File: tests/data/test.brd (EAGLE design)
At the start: 15.9 x 10.2 mm, 2 parts

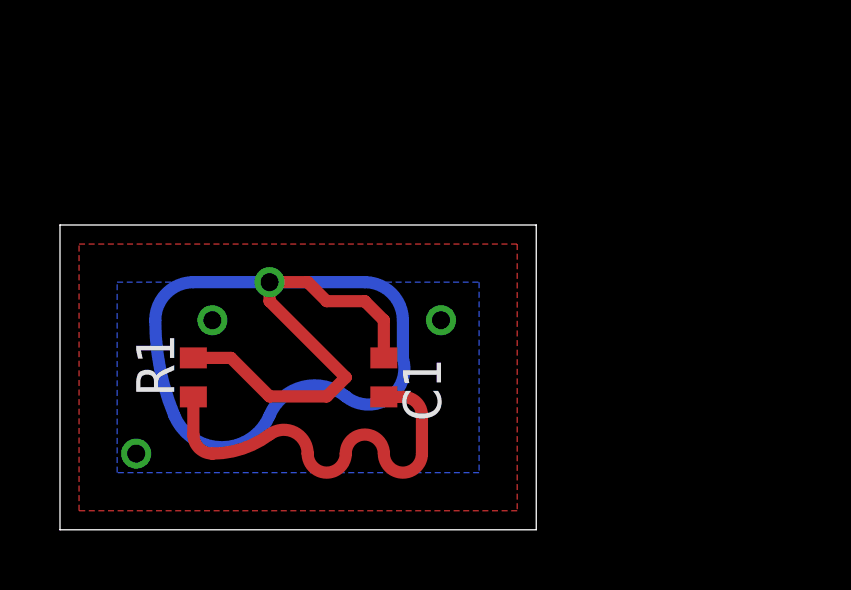
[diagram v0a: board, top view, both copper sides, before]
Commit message: Fix text center align (#14)
* Update test to detect text align error

* Treat align 'center' as 'center-center'
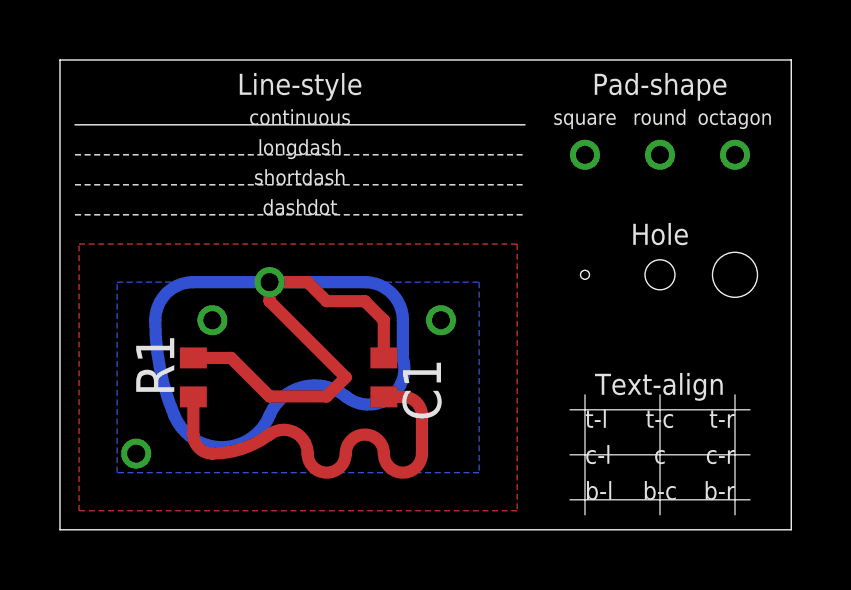
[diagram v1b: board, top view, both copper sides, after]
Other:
- board size 15.9 x 10.2 mm -> 24.4 x 15.7 mm
- board text added: "Hole"
- board text added: "Line-style"
- board text added: "Pad-shape"
- board text added: "Text-align"
- board text added: "b-c"
- board text added: "b-l"
- board text added: "b-r"
- board text added: "c"
- board text added: "c-l"
- board text added: "c-r"
- board text added: "continuous"
- board text added: "dashdot"
- board text added: "longdash"
- board text added: "octagon"
- board text added: "round"
- board text added: "shortdash"
- board text added: "square"
- board text added: "t-c"
- board text added: "t-l"
- board text added: "t-r"
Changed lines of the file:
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@@
 <setting verticaltext="up"/>
 </settings>
-<grid distance="0.05" unitdist="inch" unit="inch" style="lines" multiple="1" display="no" altdistance="0.025" altunitdist="inch" altunit="inch"/>
+<grid distance="0.5" unitdist="mm" unit="mm" style="lines" multiple="1" display="no" altdistance="0.025" altunitdist="inch" altunit="inch"/>
 <layers>
 <layer number="1" name="Top" color="4" fill="1" visible="yes" active="yes"/>
@@
 <layer number="43" name="vRestrict" color="2" fill="10" visible="yes" active="yes"/>
 <layer number="44" name="Drills" color="7" fill="1" visible="no" active="yes"/>
-<layer number="45" name="Holes" color="7" fill="1" visible="no" active="yes"/>
+<layer number="45" name="Holes" color="7" fill="1" visible="yes" active="yes"/>
 <layer number="46" name="Milling" color="3" fill="1" visible="no" active="yes"/>
 <layer number="47" name="Measures" color="7" fill="1" visible="no" active="yes"/>
@@
 <board>
 <plain>
-<wire x1="0" y1="0" x2="15.875" y2="0" width="0" layer="20"/>
-<wire x1="15.875" y1="0" x2="15.875" y2="10.16" width="0" layer="20"/>
-<wire x1="15.875" y1="10.16" x2="0" y2="10.16" width="0" layer="20"/>
-<wire x1="0" y1="10.16" x2="0" y2="0" width="0" layer="20"/>
+<wire x1="0" y1="0" x2="24.375" y2="0" width="0" layer="20"/>
+<wire x1="24.375" y1="0" x2="24.375" y2="15.66" width="0" layer="20"/>
+<wire x1="24.375" y1="15.66" x2="0" y2="15.66" width="0" layer="20"/>
+<wire x1="0" y1="15.66" x2="0" y2="0" width="0" layer="20"/>
+<text x="17.5" y="4" size="0.6" layer="21" align="top-left">t-l</text>
+<wire x1="17.5" y1="4.5" x2="17.5" y2="0.5" width="0.02" layer="21"/>
+<wire x1="20" y1="4.5" x2="20" y2="0.5" width="0.02" layer="21"/>
+<wire x1="22.5" y1="4.5" x2="22.5" y2="0.5" width="0.02" layer="21"/>
+<wire x1="17" y1="4" x2="23" y2="4" width="0.02" layer="21"/>
+<wire x1="17" y1="2.5" x2="23" y2="2.5" width="0.02" layer="21"/>
+<wire x1="17" y1="1" x2="23" y2="1" width="0.02" layer="21"/>
+<text x="17.5" y="2.5" size="0.6" layer="21" align="center-left">c-l</text>
+<text x="17.5" y="1" size="0.6" layer="21">b-l</text>
+<text x="20" y="4" size="0.6" layer="21" align="top-center">t-c</text>
+<text x="20" y="2.5" size="0.6" layer="21" align="center">c</text>
+<text x="20" y="1" size="0.6" layer="21" align="bottom-center">b-c</text>
+<text x="22.5" y="4" size="0.6" layer="21" align="top-right">t-r</text>
+<text x="22.5" y="2.5" size="0.6" layer="21" align="center-right">c-r</text>
+<text x="22.5" y="1" size="0.6" layer="21" align="bottom-right">b-r</text>
+<text x="20" y="4.5" size="0.7" layer="21" align="bottom-center">Text-align</text>
+<text x="8" y="14.5" size="0.7" layer="21" align="bottom-center">Line-style</text>
+<wire x1="0.5" y1="12.5" x2="15.5" y2="12.5" width="0.05" layer="21" style="longdash"/>
+<wire x1="0.5" y1="11.5" x2="15.5" y2="11.5" width="0.05" layer="21" style="shortdash"/>
+<wire x1="0.5" y1="10.5" x2="15.5" y2="10.5" width="0.05" layer="21" style="dashdot"/>
+<wire x1="0.5" y1="13.5" x2="15.5" y2="13.5" width="0.05" layer="21"/>
+<text x="8" y="13.5" size="0.5" layer="21" align="bottom-center">continuous</text>
+<text x="8" y="12.5" size="0.5" layer="21" align="bottom-center">longdash</text>
+<text x="8" y="11.5" size="0.5" layer="21" align="bottom-center">shortdash</text>
+<text x="8" y="10.5" size="0.5" layer="21" align="bottom-center">dashdot</text>
+<text x="20" y="14.5" size="0.7" layer="21" align="bottom-center">Pad-shape</text>
+<text x="17.5" y="13.5" size="0.5" layer="21" align="bottom-center">square</text>
+<text x="20" y="13.5" size="0.5" layer="21" align="bottom-center">round</text>
+<text x="22.5" y="13.5" size="0.5" layer="21" align="bottom-center">octagon</text>
+<hole x="20" y="8.5" drill="1"/>
+<text x="20" y="9.5" size="0.7" layer="21" align="bottom-center">Hole</text>
+<hole x="17.5" y="8.5" drill="0.3"/>
+<hole x="22.5" y="8.5" drill="1.5"/>
 </plain>
 <attributes>
@@
 <vertex x="1.905" y="1.905"/>
 </polygon>
-<via x="2.54" y="2.54" extent="1-16" drill="0.6" shape="octagon"/>
+<via x="2.54" y="2.54" extent="1-16" drill="0.6"/>
 <via x="12.7" y="6.985" extent="1-16" drill="0.6"/>
 <via x="5.08" y="6.985" extent="1-16" drill="0.6"/>
 </signal>
+<signal name="N$3">
+<via x="17.5" y="12.5" extent="1-16" drill="0.6" shape="square"/>
+</signal>
+<signal name="N$4">
+<via x="20" y="12.5" extent="1-16" drill="0.6"/>
+</signal>
+<signal name="N$5">
+<via x="22.5" y="12.5" extent="1-16" drill="0.6" shape="octagon"/>
+</signal>
 </signals>

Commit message: Support long pad (#17)
* Render long and offset pad
* Fix pad rotate
* Update test data
* Add rotated pad to test data
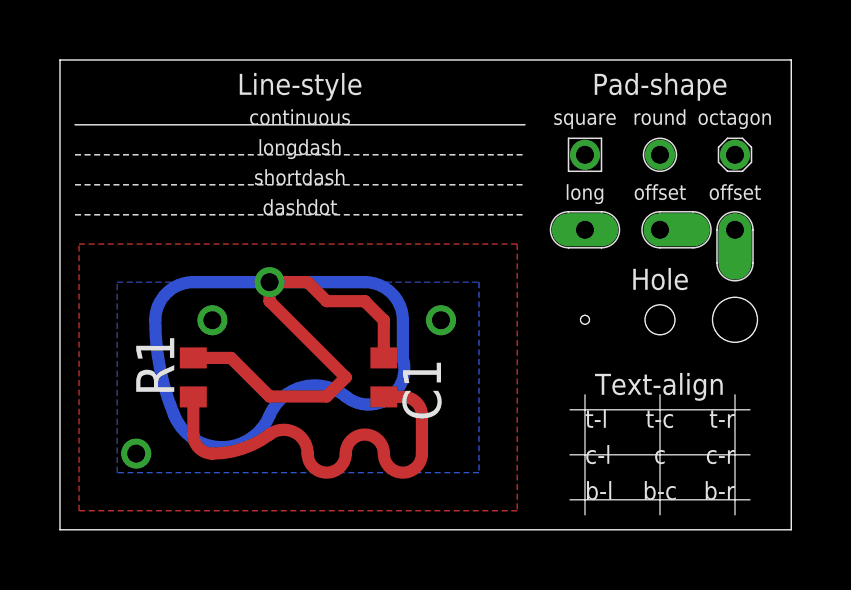
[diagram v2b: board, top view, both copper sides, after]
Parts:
- added PAD1: PADLONG, pad:LONG
- added PAD2, PAD3: PADOFFSET, pad:OFFSET
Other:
- board text added: "long"
- board text added: "offset"
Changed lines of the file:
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@@
 <setting verticaltext="up"/>
 </settings>
-<grid distance="0.5" unitdist="mm" unit="mm" style="lines" multiple="1" display="no" altdistance="0.025" altunitdist="inch" altunit="inch"/>
+<grid distance="0.05" unitdist="mm" unit="mm" style="lines" multiple="1" display="no" altdistance="0.025" altunitdist="inch" altunit="inch"/>
 <layers>
 <layer number="1" name="Top" color="4" fill="1" visible="yes" active="yes"/>
@@
 <text x="20" y="13.5" size="0.5" layer="21" align="bottom-center">round</text>
 <text x="22.5" y="13.5" size="0.5" layer="21" align="bottom-center">octagon</text>
-<hole x="20" y="8.5" drill="1"/>
-<text x="20" y="9.5" size="0.7" layer="21" align="bottom-center">Hole</text>
-<hole x="17.5" y="8.5" drill="0.3"/>
-<hole x="22.5" y="8.5" drill="1.5"/>
+<hole x="20" y="7" drill="1"/>
+<text x="20" y="8" size="0.7" layer="21" align="bottom-center">Hole</text>
+<hole x="17.5" y="7" drill="0.3"/>
+<hole x="22.5" y="7" drill="1.5"/>
+<text x="17.5" y="11" size="0.5" layer="21" align="bottom-center">long</text>
+<text x="20" y="11" size="0.5" layer="21" align="bottom-center">offset</text>
+<text x="22.5" y="11" size="0.5" layer="21" align="bottom-center">offset</text>
+<wire x1="23.1" y1="10" x2="23.1" y2="8.9" width="0.05" layer="21"/>
+<wire x1="23.1" y1="8.9" x2="21.9" y2="8.9" width="0.05" layer="21" curve="-180"/>
+<wire x1="21.9" y1="8.9" x2="21.9" y2="10" width="0.05" layer="21"/>
+<wire x1="21.9" y1="10" x2="23.1" y2="10" width="0.05" layer="21" curve="-180"/>
+<wire x1="20" y1="10.6" x2="21.1" y2="10.6" width="0.05" layer="21"/>
+<wire x1="21.1" y1="10.6" x2="21.1" y2="9.4" width="0.05" layer="21" curve="-180"/>
+<wire x1="21.1" y1="9.4" x2="20" y2="9.4" width="0.05" layer="21"/>
+<wire x1="20" y1="9.4" x2="20" y2="10.6" width="0.05" layer="21" curve="-180"/>
+<wire x1="16.95" y1="10.6" x2="18.05" y2="10.6" width="0.05" layer="21"/>
+<wire x1="18.05" y1="10.6" x2="18.05" y2="9.4" width="0.05" layer="21" curve="-180"/>
+<wire x1="18.05" y1="9.4" x2="16.95" y2="9.4" width="0.05" layer="21"/>
+<wire x1="16.95" y1="9.4" x2="16.95" y2="10.6" width="0.05" layer="21" curve="-180"/>
+<wire x1="16.95" y1="13.05" x2="18.05" y2="13.05" width="0.05" layer="21"/>
+<wire x1="18.05" y1="13.05" x2="18.05" y2="11.95" width="0.05" layer="21"/>
+<wire x1="18.05" y1="11.95" x2="16.95" y2="11.95" width="0.05" layer="21"/>
+<wire x1="16.95" y1="11.95" x2="16.95" y2="13.05" width="0.05" layer="21"/>
+<wire x1="19.45" y1="12.5" x2="20.55" y2="12.5" width="0.05" layer="21" curve="-180"/>
+<wire x1="20.55" y1="12.5" x2="19.45" y2="12.5" width="0.05" layer="21" curve="-180"/>
+<wire x1="22.25" y1="13.05" x2="22.75" y2="13.05" width="0.05" layer="21"/>
+<wire x1="22.75" y1="13.05" x2="23.05" y2="12.75" width="0.05" layer="21"/>
+<wire x1="23.05" y1="12.75" x2="23.05" y2="12.25" width="0.05" layer="21"/>
+<wire x1="23.05" y1="12.25" x2="22.75" y2="11.95" width="0.05" layer="21"/>
+<wire x1="22.75" y1="11.95" x2="22.25" y2="11.95" width="0.05" layer="21"/>
+<wire x1="22.25" y1="11.95" x2="21.95" y2="12.25" width="0.05" layer="21"/>
+<wire x1="21.95" y1="12.25" x2="21.95" y2="12.75" width="0.05" layer="21"/>
+<wire x1="21.95" y1="12.75" x2="22.25" y2="13.05" width="0.05" layer="21"/>
 </plain>
 <attributes>
@@
 <element name="C1" library="rcl" package="C0402" value="1u" x="10.795" y="5.08" rot="R270"/>
 <element name="R1" library="rcl" package="R0402" value="1k" x="4.445" y="5.08" rot="R90"/>
+<element name="PAD1" library="pad" package="LONG" value="PADLONG" x="17.5" y="10"/>
+<element name="PAD2" library="pad" package="OFFSET" value="PADOFFSET" x="20" y="10"/>
+<element name="PAD3" library="pad" package="OFFSET" value="PADOFFSET" x="22.5" y="10" rot="R270"/>
 </elements>
 <signals>
